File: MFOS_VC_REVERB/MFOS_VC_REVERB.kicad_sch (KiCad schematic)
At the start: 85 parts, among them J1 Barrel_Jack, J2 Barrel_Jack, J3 Barrel_Jack, J4 Barrel_Jack, Q1 2N3906, Q2 2N3906, U1 LM386, U2 LF411, U3 TL074, U4 LM13700, U5 TL072, U6 TL072

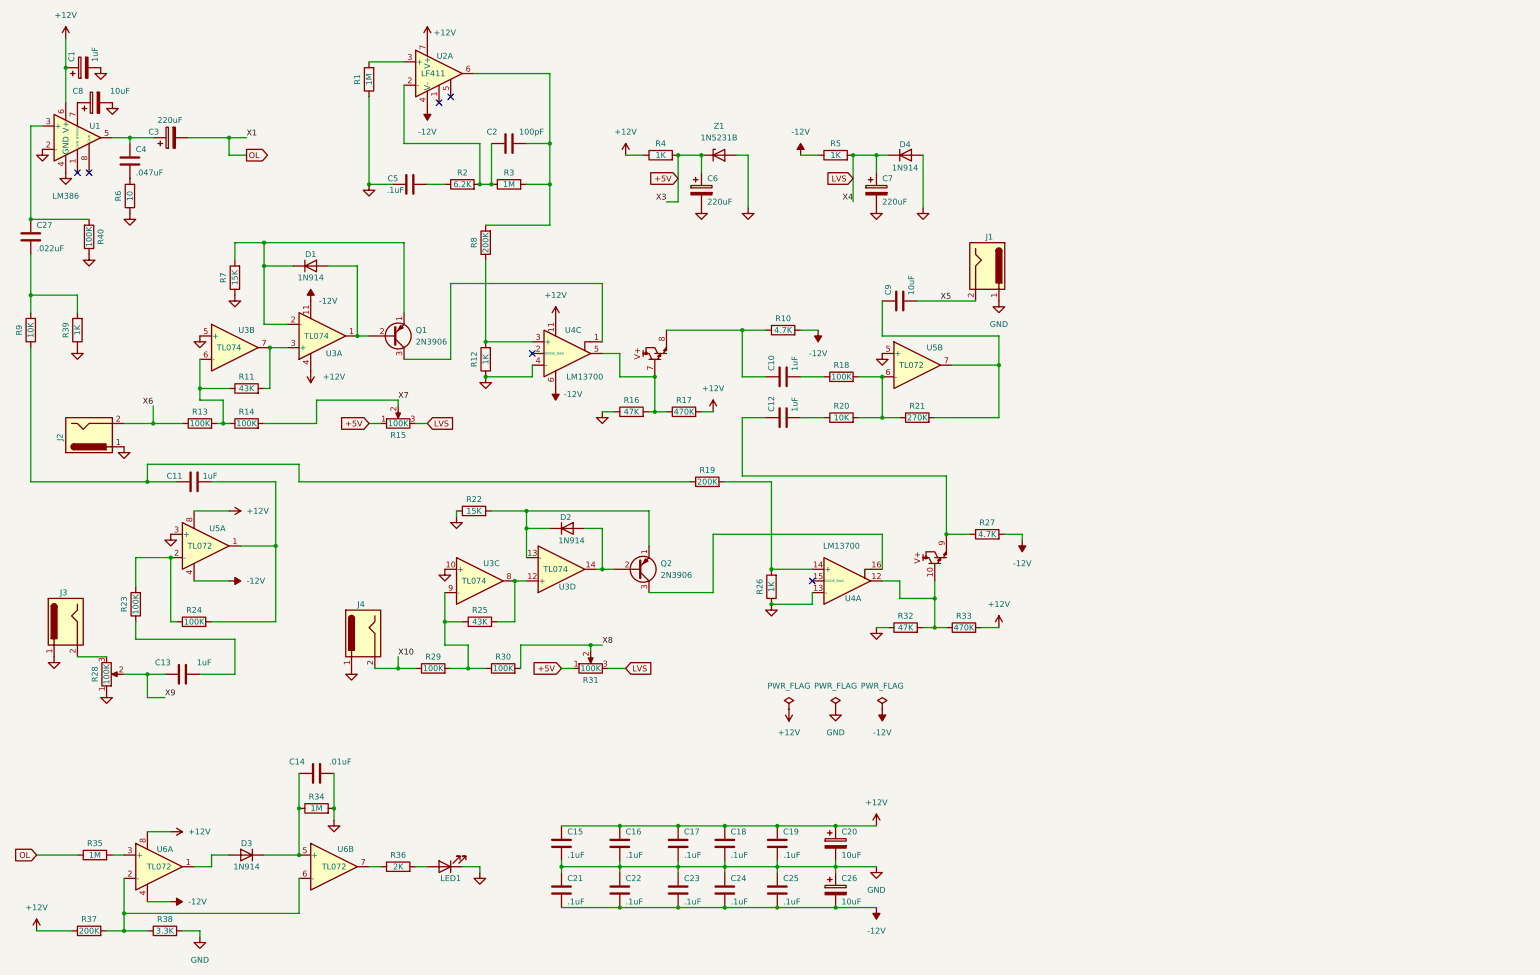
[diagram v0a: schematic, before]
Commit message: Updated BOM, renamed VCO > MFOS_VCO
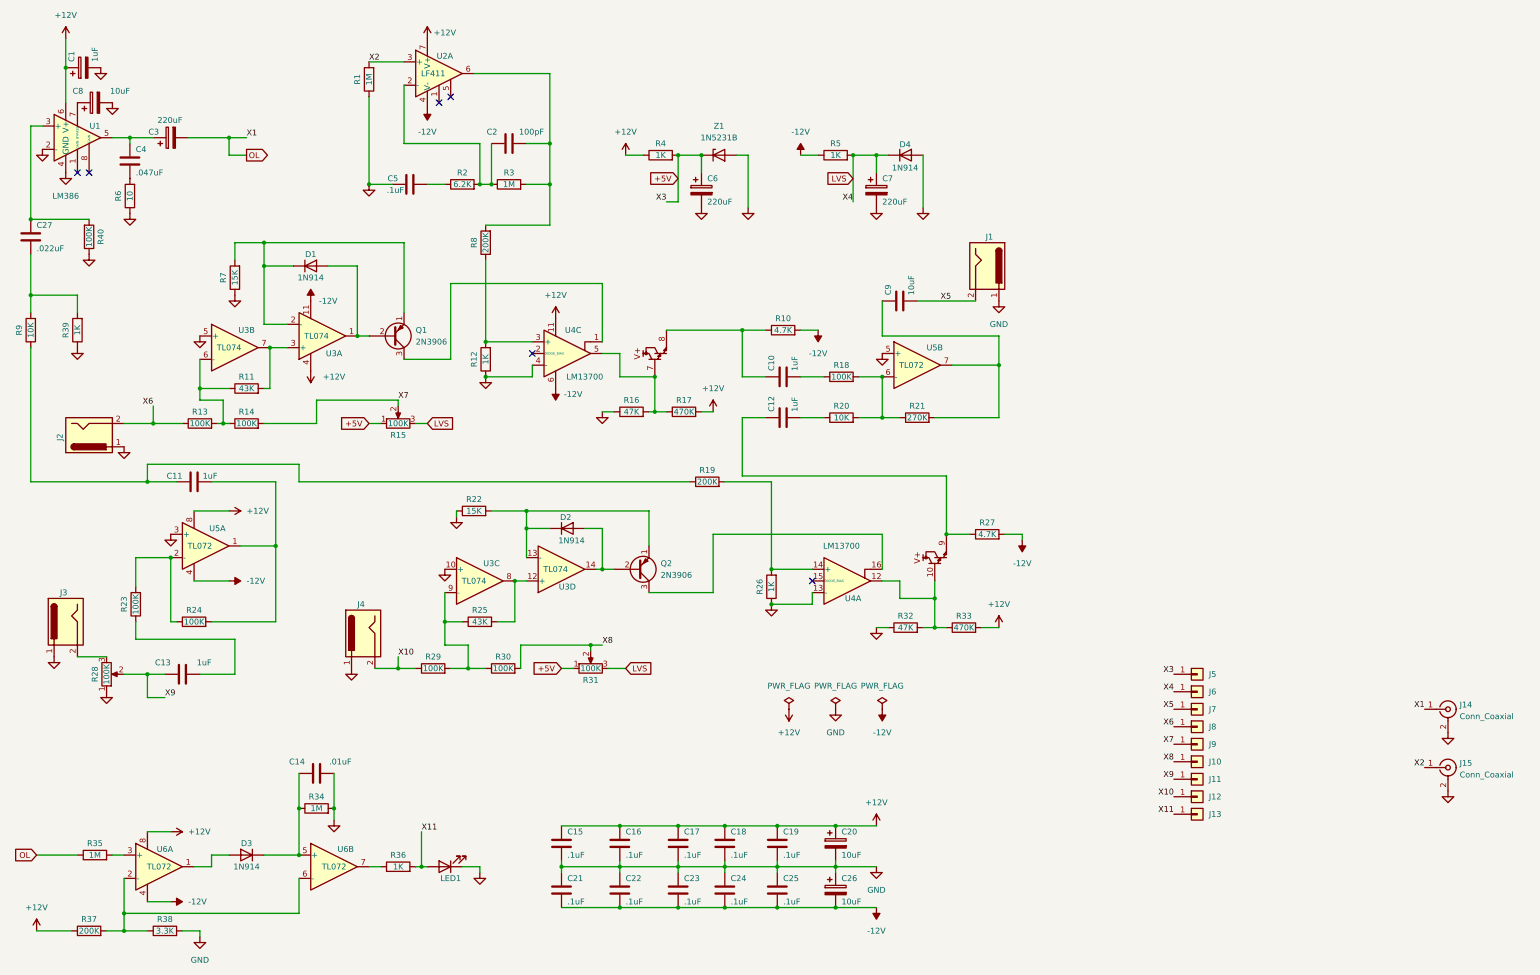
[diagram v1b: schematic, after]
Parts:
- added J10, J11, J12, J13, J5, J6, J7, J8, J9: Conn_01x01, symbol Connector_Generic:Conn_01x01
- added J14, J15: Conn_Coaxial, symbol Connector:Conn_Coaxial
- R36: value 2K -> 1K
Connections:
- net +5V: now also J5.1 (Pin_1)
- net GND: now also J14.2 (Ext), J15.2 (Ext)
- net LVS: now also J6.1 (Pin_1)
- net OL: now also J14.1 (In)
- net X10: now also J12.1 (Pin_1)
- net X5: now also J7.1 (Pin_1)
- net X6: now also J8.1 (Pin_1)
- net X7: now also J9.1 (Pin_1)
- net X8: now also J10.1 (Pin_1)
- net X9: now also J11.1 (Pin_1)
- net X11: now reaches LED1.2 (A), R36.2
- net X11: now also J13.1 (Pin_1)
- net X2: now reaches R1.2, U2.3 (+)
- net X2: now also J15.1 (In)

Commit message: Reviewed BOM
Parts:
- C1: symbol Device:C_Polarized -> dhk:C_Tantalum
- C10, C11, C12, C13, C9: symbol Device:C -> dhk:C_Alu_Bipolar
- J1, J2, J3, J4: symbol Connector:Barrel_Jack -> Connector:Jack-DC
- J10, J11, J12, J13, J5, J6, J7, J8, J9: now left out of the parts list

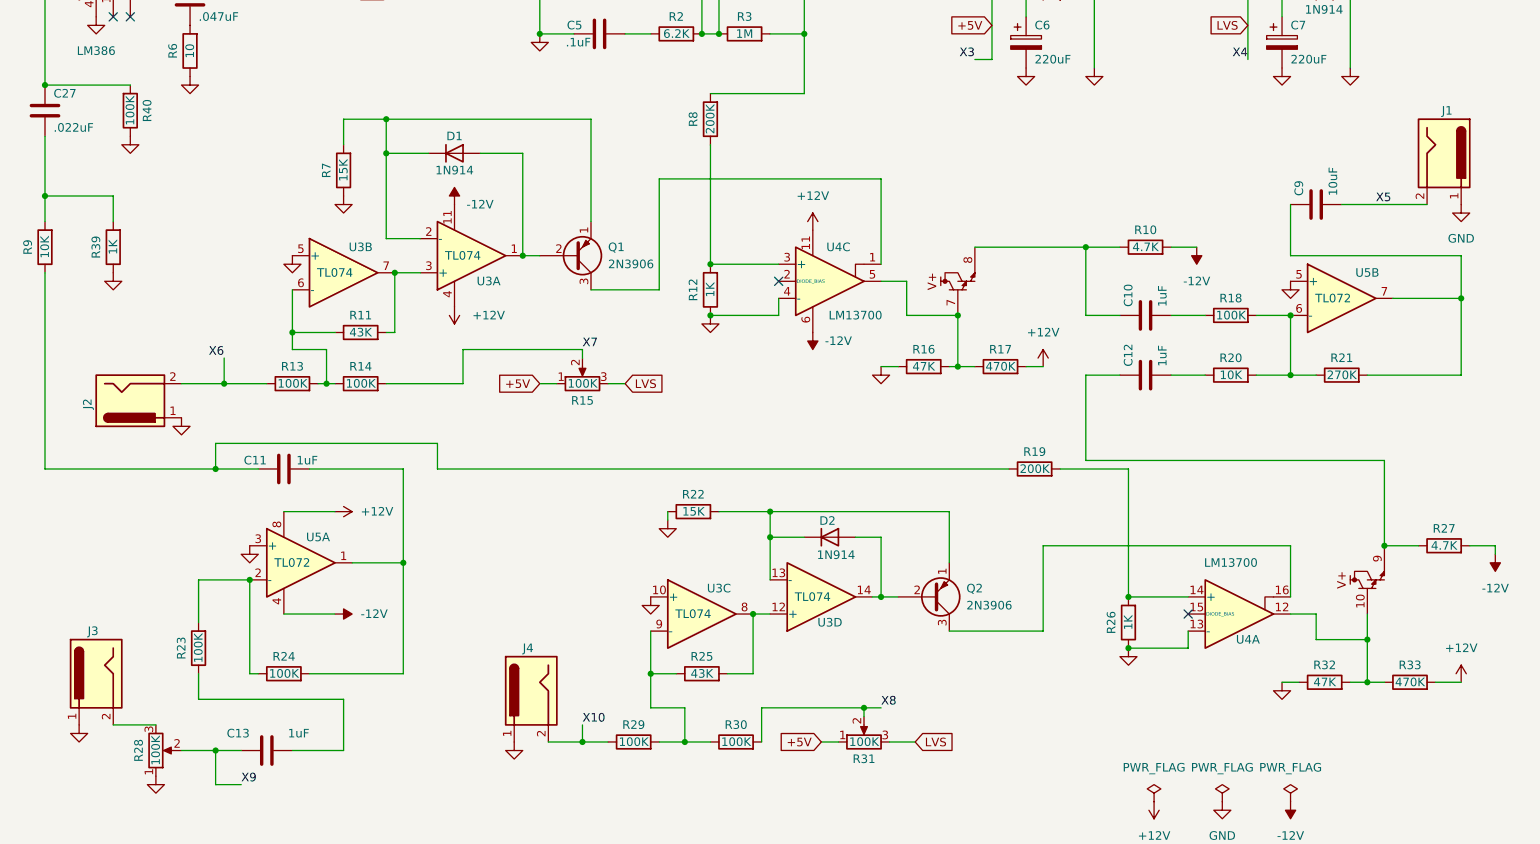
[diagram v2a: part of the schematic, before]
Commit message: Designs adapted for BOM
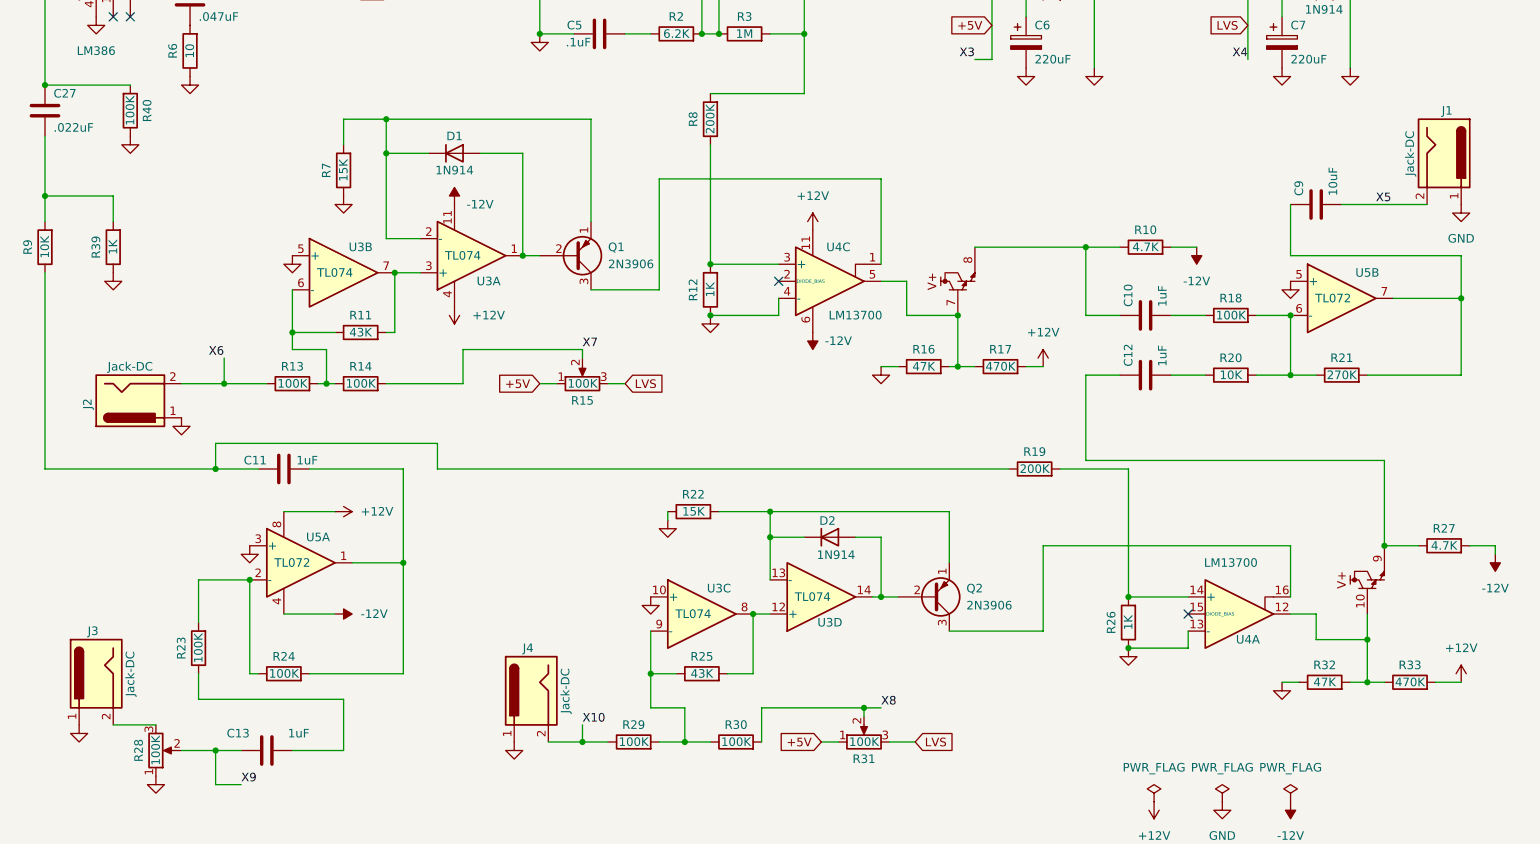
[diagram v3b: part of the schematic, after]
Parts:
- J1, J2, J3, J4: value Barrel_Jack -> Jack-DC
- LED1: value LED1 -> LED
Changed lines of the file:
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@@
       (effects (font (size 1.27 1.27)) (justify right))
     )
-    (property "Value" "Barrel_Jack" (id 1) (at 234.95 72.3899 90)
-      (effects (font (size 1.27 1.27)) (justify right) hide)
-    )
+    (property "Value" "Jack-DC" (id 1) (at 236.22 71.12 0))
     (property "Footprint" "" (id 2) (at 240.284 72.39 0)
       (effects (font (size 1.27 1.27)) hide)
@@
       (effects (font (size 1.27 1.27)) (justify right))
     )
-    (property "Value" "Barrel_Jack" (id 1) (at 46.99 149.8599 90)
-      (effects (font (size 1.27 1.27)) (justify right) hide)
-    )
+    (property "Value" "Jack-DC" (id 1) (at 45.72 148.59 0))
     (property "Footprint" "" (id 2) (at 41.656 149.86 0)
       (effects (font (size 1.27 1.27)) hide)
@@
       (effects (font (size 1.27 1.27)) (justify right))
     )
-    (property "Value" "Barrel_Jack" (id 1) (at 111.76 152.3999 90)
-      (effects (font (size 1.27 1.27)) (justify right) hide)
-    )
+    (property "Value" "Jack-DC" (id 1) (at 110.49 151.13 0))
     (property "Footprint" "" (id 2) (at 106.426 152.4 0)
       (effects (font (size 1.27 1.27)) hide)
@@
     (in_bom yes) (on_board yes)
     (property "Reference" "LED1" (id 0) (at 124.46 204.47 0))
-    (property "Value" "LED1" (id 1) (at 124.7775 205.74 0)
+    (property "Value" "LED" (id 1) (at 124.7775 205.74 0)
       (effects (font (size 1.27 1.27)) hide)
     )
@@
       (effects (font (size 1.27 1.27)) (justify right))
     )
-    (property "Value" "Barrel_Jack" (id 1) (at 46.9899 101.6 90)
-      (effects (font (size 1.27 1.27)) (justify right) hide)
-    )
+    (property "Value" "Jack-DC" (id 1) (at 45.72 102.87 0))
     (property "Footprint" "" (id 2) (at 46.99 106.934 0)
       (effects (font (size 1.27 1.27)) hide)
@@
     )
     (path "/21762559-bbc7-4c4c-bc87-f7e5de78c021"
-      (reference "J1") (unit 1) (value "Barrel_Jack") (footprint "")
+      (reference "J1") (unit 1) (value "Jack-DC") (footprint "")
     )
     (path "/f215c7a1-780b-4b2f-80e4-69d52e046a20"
-      (reference "J2") (unit 1) (value "Barrel_Jack") (footprint "")
+      (reference "J2") (unit 1) (value "Jack-DC") (footprint "")
     )
     (path "/27e84cd8-bc40-4382-a5b9-56e118596adb"
-      (reference "J3") (unit 1) (value "Barrel_Jack") (footprint "")
+      (reference "J3") (unit 1) (value "Jack-DC") (footprint "")
     )
     (path "/782c88b5-a5f2-48a4-a2c7-5fee38eec55c"
-      (reference "J4") (unit 1) (value "Barrel_Jack") (footprint "")
+      (reference "J4") (unit 1) (value "Jack-DC") (footprint "")
     )
     (path "/4ed88909-fcaf-4ca8-9b66-09ee40334cb2"
@@
     )
     (path "/dbeb0aeb-db00-4aa9-b9b1-057002484214"
-      (reference "LED1") (unit 1) (value "LED1") (footprint "")
+      (reference "LED1") (unit 1) (value "LED") (footprint "")
     )
     (path "/02265850-25bf-429b-8442-480b198625c9"
